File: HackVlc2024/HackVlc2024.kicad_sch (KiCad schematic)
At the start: 10 parts, among them J1 ESP32_IZQ, J10 LDR, J2 ESP32_DER, J3 Neopixel, J4 Lamas, J5 Suelo, J6 DH11, J7 Bomba, J8 Bomba, J9 Entrada Alimentación

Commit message: Casi las 12
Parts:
- J1: renamed from J9; footprint (none) -> Connector_PinHeader_2.54mm:PinHeader_1x02_P2.54mm_Vertical
- J2: renamed from J1; footprint (none) -> Connector_PinHeader_2.54mm:PinHeader_1x15_P2.54mm_Vertical
- J3: renamed from J2; footprint (none) -> Connector_PinHeader_2.54mm:PinHeader_1x15_P2.54mm_Vertical
- renumbered J3 to J4, J4 to J5, J7 to J6, J5 to J7, J6 to J8, J8 to J9
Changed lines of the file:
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@@
 		(on_board yes)
 		(dnp no)
-		(property "Reference" "#PWR03"
+		(property "Reference" "#PWR05"
 			(at 53.975 25.4 0)
 			(effects
@@
 			(project "HackVlc2024"
 				(path "/5ba0ba7d-dd7c-41cf-9b64-97e962dc94ab"
-					(reference "#PWR03")
+					(reference "#PWR05")
 					(unit 1)
 				)
@@
 		(on_board yes)
 		(dnp no)
-		(property "Reference" "#PWR02"
+		(property "Reference" "#PWR01"
 			(at 13.97 26.035 0)
 			(effects
@@
 			(project "HackVlc2024"
 				(path "/5ba0ba7d-dd7c-41cf-9b64-97e962dc94ab"
-					(reference "#PWR02")
+					(reference "#PWR01")
 					(unit 1)
 				)
@@
 		(on_board yes)
 		(dnp no)
-		(property "Reference" "#PWR018"
+		(property "Reference" "#PWR04"
 			(at 28.448 76.454 0)
 			(effects
@@
 			(project "HackVlc2024"
 				(path "/5ba0ba7d-dd7c-41cf-9b64-97e962dc94ab"
-					(reference "#PWR018")
+					(reference "#PWR04")
 					(unit 1)
 				)
@@
 		(dnp no)
 		(fields_autoplaced yes)
-		(property "Reference" "J6"
-			(at 99.314 53.8479 0)
+		(property "Reference" "J8"
+			(at 99.06 53.8479 0)
 			(effects
 				(font
@@
 		)
 		(property "Value" "DH11"
-			(at 99.314 56.3879 0)
+			(at 99.06 56.3879 0)
 			(effects
 				(font
@@
 			(project "HackVlc2024"
 				(path "/5ba0ba7d-dd7c-41cf-9b64-97e962dc94ab"
-					(reference "J6")
+					(reference "J8")
 					(unit 1)
 				)
@@
 		(on_board yes)
 		(dnp no)
-		(property "Reference" "J9"
+		(property "Reference" "J1"
 			(at 15.24 68.072 0)
 			(effects
@@
 			)
 		)
-		(property "Footprint" ""
+		(property "Footprint" "Connector_PinHeader_2.54mm:PinHeader_1x02_P2.54mm_Vertical"
 			(at 15.494 76.454 0)
 			(effects
@@
 			(project "HackVlc2024"
 				(path "/5ba0ba7d-dd7c-41cf-9b64-97e962dc94ab"
-					(reference "J9")
+					(reference "J1")
 					(unit 1)
 				)
@@
 		(on_board yes)
 		(dnp no)
-		(property "Reference" "#PWR05"
+		(property "Reference" "#PWR07"
 			(at 66.802 25.146 0)
 			(effects
@@
 			(project "HackVlc2024"
 				(path "/5ba0ba7d-dd7c-41cf-9b64-97e962dc94ab"
-					(reference "#PWR05")
+					(reference "#PWR07")
 					(unit 1)
 				)
@@
 		(dnp no)
 		(fields_autoplaced yes)
-		(property "Reference" "J4"
-			(at 101.092 23.8759 0)
+		(property "Reference" "J5"
+			(at 101.6 23.8759 0)
 			(effects
 				(font
@@
 		)
 		(property "Value" "Lamas"
-			(at 101.092 26.4159 0)
+			(at 101.6 26.4159 0)
 			(effects
 				(font
@@
 			(project "HackVlc2024"
 				(path "/5ba0ba7d-dd7c-41cf-9b64-97e962dc94ab"
-					(reference "J4")
+					(reference "J5")
 					(unit 1)
 				)
@@
 		(on_board yes)
 		(dnp no)
-		(property "Reference" "#PWR04"
+		(property "Reference" "#PWR06"
 			(at 61.595 26.035 0)
 			(effects
@@
 			(project "HackVlc2024"
 				(path "/5ba0ba7d-dd7c-41cf-9b64-97e962dc94ab"
-					(reference "#PWR04")
+					(reference "#PWR06")
 					(unit 1)
 				)
@@
 		(on_board yes)
 		(dnp no)
-		(property "Reference" "#PWR016"
+		(property "Reference" "#PWR018"
 			(at 111.76 65.278 0)
 			(effects
@@
 			(project "HackVlc2024"
 				(path "/5ba0ba7d-dd7c-41cf-9b64-97e962dc94ab"
-					(reference "#PWR016")
+					(reference "#PWR018")
 					(unit 1)
 				)
@@
 		(dnp no)
 		(fields_autoplaced yes)
-		(property "Reference" "J7"
-			(at 122.682 23.8759 0)
+		(property "Reference" "J6"
+			(at 123.19 23.8759 0)
 			(effects
 				(font
@@
 		)
 		(property "Value" "Bomba"
-			(at 122.682 26.4159 0)
+			(at 123.19 26.4159 0)
 			(effects
 				(font
@@
 			(project "HackVlc2024"
 				(path "/5ba0ba7d-dd7c-41cf-9b64-97e962dc94ab"
-					(reference "J7")
+					(reference "J6")
 					(unit 1)
 				)
@@
 		(on_board yes)
 		(dnp no)
-		(property "Reference" "J2"
+		(property "Reference" "J3"
 			(at 42.545 33.147 0)
 			(effects
@@
 			)
 		)
-		(property "Footprint" ""
+		(property "Footprint" "Connector_PinHeader_2.54mm:PinHeader_1x15_P2.54mm_Vertical"
 			(at 46.355 41.275 0)
 			(effects
@@
 			(project "HackVlc2024"
 				(path "/5ba0ba7d-dd7c-41cf-9b64-97e962dc94ab"
-					(reference "J2")
+					(reference "J3")
 					(unit 1)
 				)
@@
 		(dnp no)
 		(fields_autoplaced yes)
-		(property "Reference" "J1"
+		(property "Reference" "J2"
 			(at 31.115 40.0049 0)
 			(effects
@@
 			)
 		)
-		(property "Footprint" ""
+		(property "Footprint" "Connector_PinHeader_2.54mm:PinHeader_1x15_P2.54mm_Vertical"
 			(at 28.575 41.275 0)
 			(effects
@@
 			(project "HackVlc2024"
 				(path "/5ba0ba7d-dd7c-41cf-9b64-97e962dc94ab"
-					(reference "J1")
+					(reference "J2")
 					(unit 1)
 				)
@@
 		(on_board yes)
 		(dnp no)
-		(property "Reference" "#PWR015"
+		(property "Reference" "#PWR017"
 			(at 111.76 52.578 0)
 			(effects
@@
 			(project "HackVlc2024"
 				(path "/5ba0ba7d-dd7c-41cf-9b64-97e962dc94ab"
-					(reference "#PWR015")
+					(reference "#PWR017")
 					(unit 1)
 				)
@@
 		(dnp no)
 		(fields_autoplaced yes)
-		(property "Reference" "J5"
-			(at 78.232 53.8479 0)
+		(property "Reference" "J7"
+			(at 78.74 53.8479 0)
 			(effects
 				(font
@@
 		)
 		(property "Value" "Suelo"
-			(at 78.232 56.3879 0)
+			(at 78.74 56.3879 0)
 			(effects
 				(font
@@
 			(project "HackVlc2024"
 				(path "/5ba0ba7d-dd7c-41cf-9b64-97e962dc94ab"
-					(reference "J5")
+					(reference "J7")
 					(unit 1)
 				)
@@
 		(on_board yes)
 		(dnp no)
-		(property "Reference" "#PWR017"
+		(property "Reference" "#PWR03"
 			(at 18.288 73.914 0)
 			(effects
@@
 			(project "HackVlc2024"
 				(path "/5ba0ba7d-dd7c-41cf-9b64-97e962dc94ab"
-					(reference "#PWR017")
+					(reference "#PWR03")
 					(unit 1)
 				)
@@
 		(on_board yes)
 		(dnp no)
-		(property "Reference" "#PWR06"
+		(property "Reference" "#PWR08"
 			(at 66.802 35.306 0)
 			(effects
@@
 			(project "HackVlc2024"
 				(path "/5ba0ba7d-dd7c-41cf-9b64-97e962dc94ab"
-					(reference "#PWR06")
+					(reference "#PWR08")
 					(unit 1)
 				)
@@
 		(on_board yes)
 		(dnp no)
-		(property "Reference" "#PWR013"
+		(property "Reference" "#PWR015"
 			(at 111.252 25.146 0)
 			(effects
@@
 			(project "HackVlc2024"
 				(path "/5ba0ba7d-dd7c-41cf-9b64-97e962dc94ab"
-					(reference "#PWR013")
+					(reference "#PWR015")
 					(unit 1)
 				)
@@
 		(on_board yes)
 		(dnp no)
-		(property "Reference" "#PWR014"
+		(property "Reference" "#PWR016"
 			(at 111.252 35.306 0)
 			(effects
@@
 			(project "HackVlc2024"
 				(path "/5ba0ba7d-dd7c-41cf-9b64-97e962dc94ab"
-					(reference "#PWR014")
+					(reference "#PWR016")
 					(unit 1)
 				)
@@
 		(on_board yes)
 		(dnp no)
-		(property "Reference" "#PWR01"
+		(property "Reference" "#PWR02"
 			(at 21.59 26.035 0)
 			(effects
@@
 			(project "HackVlc2024"
 				(path "/5ba0ba7d-dd7c-41cf-9b64-97e962dc94ab"
-					(reference "#PWR01")
+					(reference "#PWR02")
 					(unit 1)
 				)
@@
 		(dnp no)
 		(fields_autoplaced yes)
-		(property "Reference" "J8"
+		(property "Reference" "J9"
 			(at 123.19 52.5779 0)
 			(effects
@@
 			(project "HackVlc2024"
 				(path "/5ba0ba7d-dd7c-41cf-9b64-97e962dc94ab"
-					(reference "J8")
+					(reference "J9")
 					(unit 1)
 				)
@@
 		(on_board yes)
 		(dnp no)
-		(property "Reference" "#PWR08"
+		(property "Reference" "#PWR014"
 			(at 89.662 35.306 0)
 			(effects
@@
 			(project "HackVlc2024"
 				(path "/5ba0ba7d-dd7c-41cf-9b64-97e962dc94ab"
-					(reference "#PWR08")
+					(reference "#PWR014")
 					(unit 1)
 				)
@@
 		(dnp no)
 		(fields_autoplaced yes)
-		(property "Reference" "J3"
+		(property "Reference" "J4"
 			(at 78.232 23.8759 0)
 			(effects
@@
 			(project "HackVlc2024"
 				(path "/5ba0ba7d-dd7c-41cf-9b64-97e962dc94ab"
-					(reference "J3")
+					(reference "J4")
 					(unit 1)
 				)
@@
 		(on_board yes)
 		(dnp no)
-		(property "Reference" "#PWR07"
+		(property "Reference" "#PWR013"
 			(at 89.662 25.146 0)
 			(effects
@@
 			(project "HackVlc2024"
 				(path "/5ba0ba7d-dd7c-41cf-9b64-97e962dc94ab"
-					(reference "#PWR07")
-					(unit 1)
-				)
+					(reference "#PWR013")
+					(unit 1)
+				)

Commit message: PCB acida
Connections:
- net D9 is gone; now on net D27: J5.2 (Pin_2)
- net +5V: now also J3.1 (Pin_1); no longer J3.15 (Pin_15)
- net D12: now also J3.4 (Pin_4); no longer J3.12 (Pin_12)
- net D13: now also J3.3 (Pin_3); no longer J3.13 (Pin_13)
- net D14: now also J3.5 (Pin_5); no longer J3.11 (Pin_11)
- net D26: now also J3.7 (Pin_7); no longer J3.9 (Pin_9)
- net D27: now also J3.6 (Pin_6); no longer J3.10 (Pin_10)
- net D32: now also J3.10 (Pin_10); no longer J3.6 (Pin_6)
- net D33: now also J3.9 (Pin_9); no longer J3.7 (Pin_7)
- net D34: now also J3.12 (Pin_12); no longer J3.4 (Pin_4)
- net D35: now also J3.11 (Pin_11); no longer J3.5 (Pin_5)
- net EN: now also J3.15 (Pin_15); no longer J3.1 (Pin_1)
- net GND: now also J3.2 (Pin_2); no longer J3.14 (Pin_14)
- net VN: now also J3.13 (Pin_13); no longer J3.3 (Pin_3)
- net VP: now also J3.14 (Pin_14); no longer J3.2 (Pin_2)
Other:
- company: (none) -> Hackerspace Valencia - HCH
- title: (none) -> Space Apps 2024
- moved on the sheet: J3
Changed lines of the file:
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@@
 	(generator_version "8.0")
 	(paper "A4")
+	(title_block
+		(title "Space Apps 2024")
+		(date "2024-10-05")
+		(rev "V0")
+		(company "Hackerspace Valencia - HCH")
+	)
 	(wire
 		(pts
@@
 		)
 	)
-	(label "D9"
+	(label "D27"
 		(at 89.662 25.146 0)
 		(fields_autoplaced yes)
@@
 	(symbol
 		(lib_id "Connector_Generic:Conn_01x15")
-		(at 46.355 41.275 180)
+		(at 46.355 41.275 0)
+		(mirror y)
 		(unit 1)
 		(exclude_from_sim no)
@@
 		(dnp no)
 		(property "Reference" "J3"
-			(at 42.545 33.147 0)
+			(at 42.545 49.403 0)
 			(effects
 				(font
@@
 		)
 		(property "Value" "ESP32_DER"
-			(at 38.735 35.433 0)
-			(effects
-				(font
+			(at 38.735 47.117 0)
+			(effects
+				(font

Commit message: Versión final de hoy por la mañana
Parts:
- J1: footprint Connector_PinHeader_2.54mm:PinHeader_1x02_P2.54mm_Vertical -> TerminalBlock_Phoenix:TerminalBlock_Phoenix_MKDS-1,5-2_1x02_P5.00mm_Horizontal
- J2, J3: footprint Connector_PinHeader_2.54mm:PinHeader_1x15_P2.54mm_Vertical -> Connector_PinSocket_2.54mm:PinSocket_1x15_P2.54mm_Vertical
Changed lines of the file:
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@@
 	(rectangle
 		(start 12.7 64.262)
-		(end 39.624 97.917)
+		(end 39.624 79.502)
 		(stroke
 			(width 0)
@@
 			)
 		)
-		(property "Footprint" "Connector_PinHeader_2.54mm:PinHeader_1x02_P2.54mm_Vertical"
+		(property "Footprint" "TerminalBlock_Phoenix:TerminalBlock_Phoenix_MKDS-1,5-2_1x02_P5.00mm_Horizontal"
 			(at 15.494 76.454 0)
 			(effects
@@
 			)
 		)
-		(property "Footprint" "Connector_PinHeader_2.54mm:PinHeader_1x15_P2.54mm_Vertical"
+		(property "Footprint" "Connector_PinSocket_2.54mm:PinSocket_1x15_P2.54mm_Vertical"
 			(at 46.355 41.275 0)
 			(effects
@@
 			)
 		)
-		(property "Footprint" "Connector_PinHeader_2.54mm:PinHeader_1x15_P2.54mm_Vertical"
+		(property "Footprint" "Connector_PinSocket_2.54mm:PinSocket_1x15_P2.54mm_Vertical"
 			(at 28.575 41.275 0)
 			(effects

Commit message: Pin luz a 32
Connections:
- net D25: no longer J10.2 (Pin_2)
- net D32: now also J10.2 (Pin_2)
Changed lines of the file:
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@@
 		)
 	)
-	(label "D25"
+	(label "D32"
 		(at 135.128 55.118 0)
 		(fields_autoplaced yes)

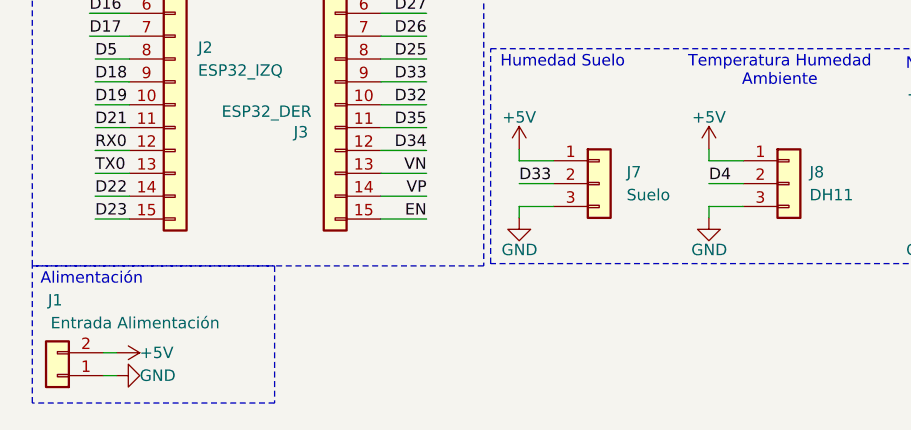
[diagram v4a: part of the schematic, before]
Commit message: Pin 4 cambiado a 34
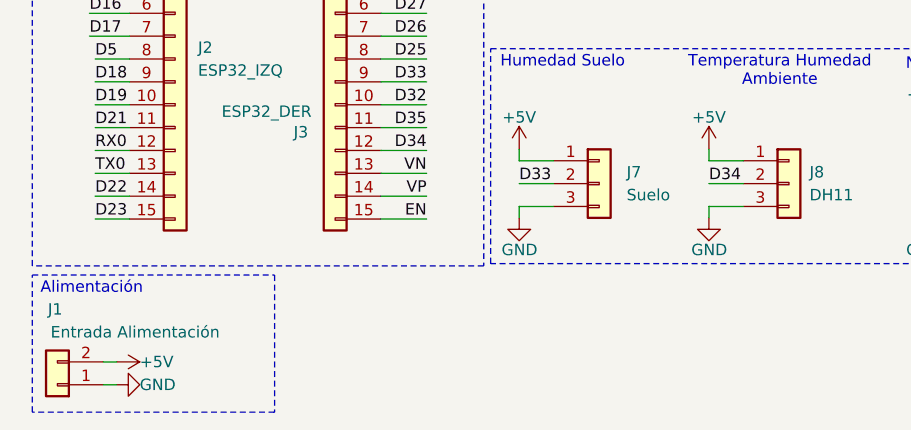
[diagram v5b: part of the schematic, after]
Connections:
- net D34: now also J8.2 (Pin_2)
- net D4: no longer J8.2 (Pin_2)
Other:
- moved on the sheet: J1
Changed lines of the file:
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@@
 	(wire
 		(pts
-			(xy 22.098 76.454) (xy 20.574 76.454)
+			(xy 22.098 77.47) (xy 20.574 77.47)
 		)
 		(stroke
@@
 	(wire
 		(pts
-			(xy 22.098 73.914) (xy 20.574 73.914)
+			(xy 22.098 74.93) (xy 20.574 74.93)
 		)
 		(stroke
@@
 	)
 	(rectangle
-		(start 12.7 64.262)
-		(end 39.624 79.502)
+		(start 12.7 65.278)
+		(end 39.624 80.518)
 		(stroke
 			(width 0)
@@
 	(text "Alimentación"
 		(exclude_from_sim no)
-		(at 19.304 65.786 0)
+		(at 19.304 66.802 0)
 		(effects
 			(font
@@
 		)
 	)
-	(label "D4"
+	(label "D34"
 		(at 87.884 55.118 0)
 		(fields_autoplaced yes)
@@
 	(symbol
 		(lib_id "power:GND")
-		(at 22.098 76.454 90)
+		(at 22.098 77.47 90)
 		(unit 1)
 		(exclude_from_sim no)
@@
 		(dnp no)
 		(property "Reference" "#PWR04"
-			(at 28.448 76.454 0)
+			(at 28.448 77.47 0)
 			(effects
 				(font
@@
 		)
 		(property "Value" "GND"
-			(at 24.638 76.454 90)
+			(at 24.638 77.47 90)
 			(effects
 				(font
@@
 		)
 		(property "Footprint" ""
-			(at 22.098 76.454 0)
+			(at 22.098 77.47 0)
 			(effects
 				(font
@@
 		)
 		(property "Datasheet" ""
-			(at 22.098 76.454 0)
+			(at 22.098 77.47 0)
 			(effects
 				(font
@@
 		)
 		(property "Description" "Power symbol creates a global label with name \"GND\" , ground"
-			(at 22.098 76.454 0)
+			(at 22.098 77.47 0)
 			(effects
 				(font
@@
 	(symbol
 		(lib_id "Connector_Generic:Conn_01x02")
-		(at 15.494 76.454 180)
+		(at 15.494 77.47 180)
 		(unit 1)
 		(exclude_from_sim no)
@@
 		(dnp no)
 		(property "Reference" "J1"
-			(at 15.24 68.072 0)
+			(at 15.24 69.088 0)
 			(effects
 				(font
@@
 		)
 		(property "Value" "Entrada Alimentación"
-			(at 24.13 70.612 0)
+			(at 24.13 71.628 0)
 			(effects
 				(font
@@
 		)
 		(property "Footprint" "TerminalBlock_Phoenix:TerminalBlock_Phoenix_MKDS-1,5-2_1x02_P5.00mm_Horizontal"
-			(at 15.494 76.454 0)
+			(at 15.494 77.47 0)
 			(effects
 				(font
@@
 		)
 		(property "Datasheet" "~"
-			(at 15.494 76.454 0)
+			(at 15.494 77.47 0)
 			(effects
 				(font
@@
 		)
 		(property "Description" "Generic connector, single row, 01x02, script generated (kicad-library-utils/schlib/autogen/connector/)"
-			(at 15.494 76.454 0)
+			(at 15.494 77.47 0)
 			(effects
 				(font
@@
 	(symbol
 		(lib_id "power:+5V")
-		(at 22.098 73.914 270)
+		(at 22.098 74.93 270)
 		(unit 1)
 		(exclude_from_sim no)
@@
 		(dnp no)
 		(property "Reference" "#PWR03"
-			(at 18.288 73.914 0)
+			(at 18.288 74.93 0)
 			(effects
 				(font
@@
 		)
 		(property "Value" "+5V"
-			(at 24.638 73.914 90)
+			(at 24.638 74.93 90)
 			(effects
 				(font
@@
 		)
 		(property "Footprint" ""
-			(at 22.098 73.914 0)
+			(at 22.098 74.93 0)
 			(effects
 				(font
@@
 		)
 		(property "Datasheet" ""
-			(at 22.098 73.914 0)
+			(at 22.098 74.93 0)
 			(effects
 				(font
@@
 		)
 		(property "Description" "Power symbol creates a global label with name \"+5V\""
-			(at 22.098 73.914 0)
-			(effects
-				(font
+			(at 22.098 74.93 0)
+			(effects
+				(font

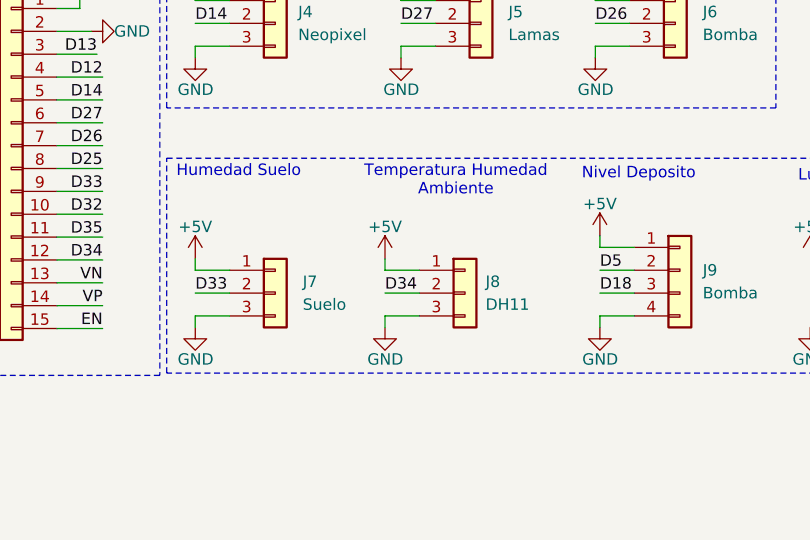
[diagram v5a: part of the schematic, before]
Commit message: D34 vuelve a ser D4
Por el DH11
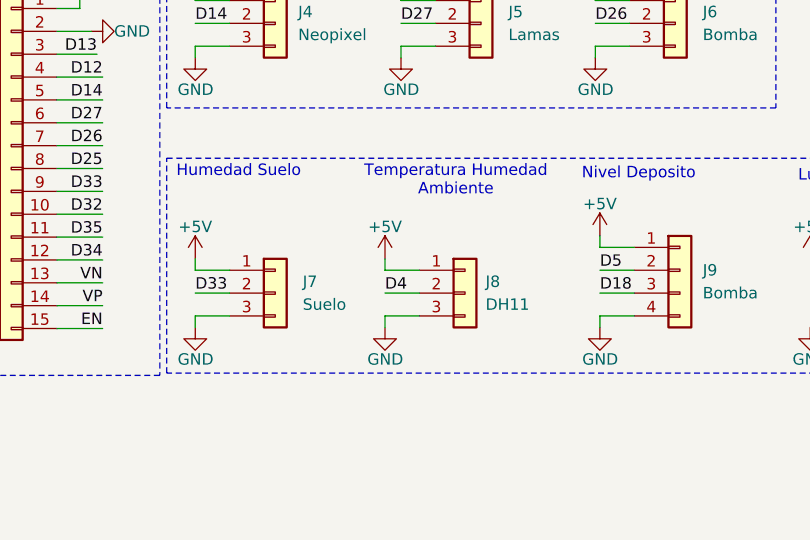
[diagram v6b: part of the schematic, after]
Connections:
- net D34: no longer J8.2 (Pin_2)
- net D4: now also J8.2 (Pin_2)
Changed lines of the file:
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@@
 		)
 	)
-	(label "D34"
+	(label "D4"
 		(at 87.884 55.118 0)
 		(fields_autoplaced yes)
